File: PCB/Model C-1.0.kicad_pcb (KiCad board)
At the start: 2 copper layers, 79.3 x 144.8 mm, 70 parts, among them J1 batt, J2 USB_C_Receptacle_PowerOnly_6P, J3 AVR-ISP-6, J4 reset, J5 boot, SW1 SW_SPST, U1 ATmega32A-A, U2 MCP73833-AMI/MF, U3 CA56-12CGKWA, U4 CA56-12CGKWA, U5 MAX7219, U6 MT3608, Y1 Crystal

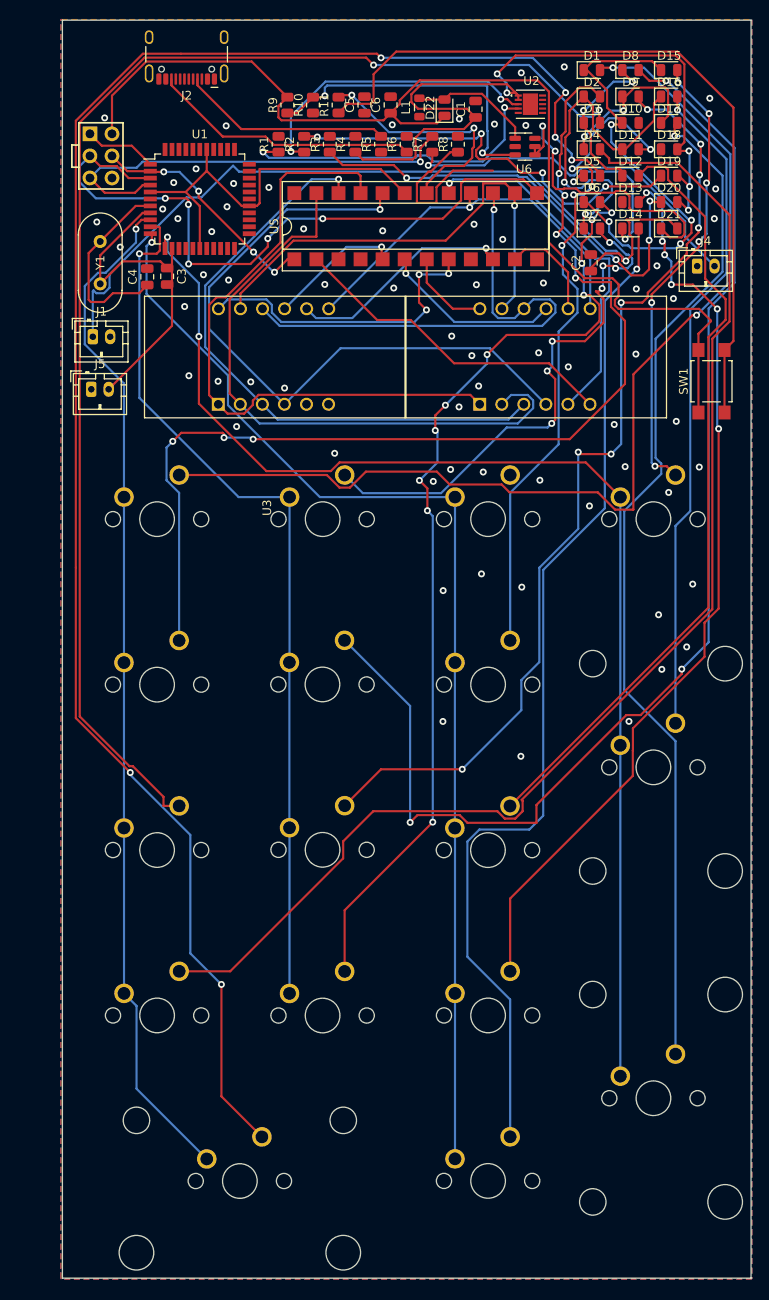
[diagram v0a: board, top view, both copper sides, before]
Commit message: swap battery
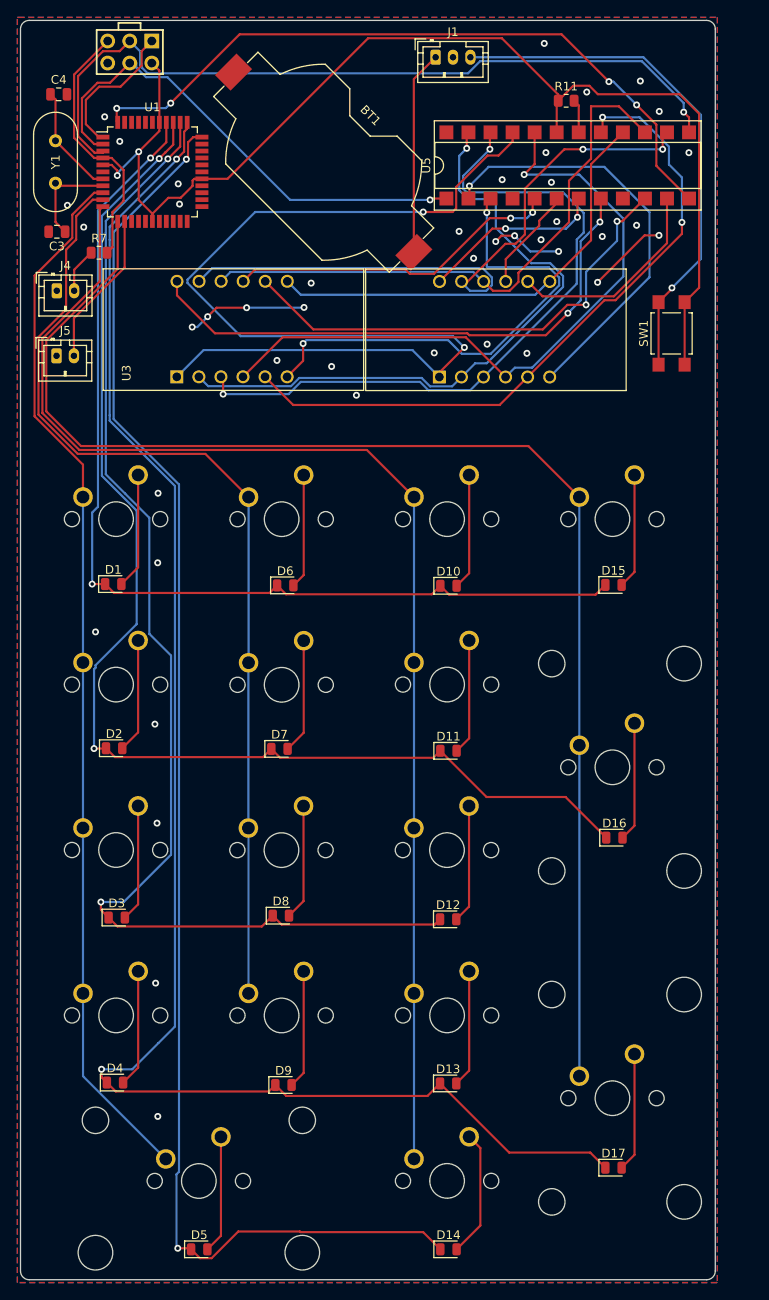
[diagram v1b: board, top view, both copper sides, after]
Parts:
- removed C1, C2: 10uF, Capacitor_SMD:C_0805_2012Metric
- removed C5, C6: 22uF, Capacitor_SMD:C_0805_2012Metric
- removed D18: GREEN, LED_SMD:LED_0805_2012Metric
- removed D19: YELLOW, LED_SMD:LED_0805_2012Metric
- removed D20: RED, LED_SMD:LED_0805_2012Metric
- removed D21: 1N4148, Diode_SMD:D_0805_2012Metric
- removed D22: D_Schottky, Diode_SMD:D_0805_2012Metric
- removed J2: USB_C_Receptacle_PowerOnly_6P, Connector_USB:USB_C_Receptacle_HCTL_HC-TYPE-C-16P-01A
- removed L1: L, Inductor_SMD:L_0805_2012Metric
- removed R1, R2, R3: 1.5k, Resistor_SMD:R_0805_2012Metric
- removed R10: 15k, Resistor_SMD:R_0805_2012Metric
- removed R4: 2k, Resistor_SMD:R_0805_2012Metric
- removed R5, R6: 5.1k, Resistor_SMD:R_0805_2012Metric
- removed R8: 10k, Resistor_SMD:R_0805_2012Metric
- removed R9: 110k, Resistor_SMD:R_0805_2012Metric
- removed U2: MCP73833-AMI/MF, footprints:DFN10_3x3MC_MCH
- removed U6: MT3608, Package_TO_SOT_SMD:SOT-23-6
- added BT1: Battery_Cell, Battery:BatteryHolder_Keystone_1058_1x2032, F.Cu at (62.2, 56.4)
- J1: value batt -> 1.5V-5V Boost Converter; footprint Connector_JST:JST_PH_B2B-PH-K_1x02_P2.00mm_Vertical -> Connector_JST:JST_PH_B3B-PH-K_1x03_P2.00mm_Vertical
- moved D5 131.6 mm to (47.9, 181.6)
- moved D4 120.7 mm to (38.2, 162.4)
- moved D9 120.6 mm to (57.6, 162.7)
- moved D17 120.5 mm to (95.6, 172.2)
- moved D14 119.4 mm to (76.6, 181.6)
- moved D3 106.6 mm to (38.4, 143.4)
- moved D8 105.4 mm to (57.3, 143.2)
- moved D13 103.6 mm to (76.6, 162.5)
- moved D2 93.0 mm to (38.1, 123.9)
- moved D12 88.2 mm to (76.6, 143.6)
- moved D16 85.6 mm to (95.7, 134.2)
- moved D1 80.9 mm to (38.0, 105.0)
- moved J4 73.8 mm to (31.5, 71.2)
- moved D11 72.4 mm to (76.6, 124.2)
- moved D7 69.9 mm to (57.1, 124.0)
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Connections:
- J3 pad 2: +5V -> /5v switched
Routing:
- net Net-(D5-Pad2): track 200.7 -> 13.6 mm, vias 6 -> 0
- net /row3: track 18.8 -> 186.5 mm
- net /row4: track 17.5 -> 168.9 mm
- net Net-(D3-Pad2): track 152.3 -> 13.5 mm, vias 2 -> 0
- net Net-(D4-Pad2): track 146.0 -> 13.5 mm
- net Net-(D8-Pad2): track 142.2 -> 13.3 mm, vias 3 -> 0
- net /row2: track 19.1 -> 143.2 mm
- net Net-(D2-Pad2): track 123.8 -> 13.2 mm, vias 7 -> 0
- net Net-(D1-Pad2): track 120.6 -> 13.4 mm, vias 2 -> 0
- net Net-(D17-Pad2): track 117.9 -> 13.7 mm, vias 1 -> 0
- net Net-(D14-Pad2): track 118.2 -> 14.6 mm, vias 1 -> 0
- net /row1: track 40.7 -> 143.9 mm
- net Net-(D9-Pad2): track 112.3 -> 13.7 mm, vias 8 -> 0
- net Net-(D6-Pad2): track 111.7 -> 13.2 mm, vias 10 -> 0
- net Net-(D13-Pad2): track 106.2 -> 13.5 mm, vias 6 -> 0
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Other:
- board size 79.3 x 144.8 mm -> 80 x 145 mm

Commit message: minor modifications
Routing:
- net GND: track 31.4 -> 61.8 mm, vias 43 -> 39
- net /c: track 77.9 -> 83.3 mm
- net /4: track 55.9 -> 53.1 mm
- net /e: track 119.2 -> 122.1 mm
- net /b: track 52.0 -> 53.7 mm
- net /g: track 79.0 -> 77.4 mm
- net /row1: track 143.9 -> 145.4 mm
- net /a: track 74.7 -> 76.1 mm
- net /5v switched: track 136.9 -> 138.2 mm
- net Net-(J4-Pin_2): track 5.19 -> 6.35 mm
- net /miso: track 16.8 -> 17.8 mm
- net /mosi: track 57.4 -> 58.3 mm
- net /3: track 21.2 -> 21.9 mm
- net /row0: track 118.3 -> 118.8 mm
